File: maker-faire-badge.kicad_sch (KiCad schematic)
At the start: 37 parts, among them J1 USB-C, Q1 2N3906, Q2 2N3906, Q3 2N3906, Q4 2N3906, Q5 2N3906, Q6 2N3906

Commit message: updated design files
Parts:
- BT1, BT2: symbol Device:Battery_Cell -> Library:Battery_Cell
- C1, C2, C3, C4, C5, C6: symbol Device:C_Polarized_US -> Library:C_Polarized_US
- D1: symbol Device:LED_BKRG -> Library:LED_BKRG
- D2: symbol Device:D_Zener -> Library:D_Zener
- D3, D4: symbol Diode:1N5822 -> Library:1N5822
- H1: symbol Mechanical:MountingHole_Pad -> Library:MountingHole_Pad
- J1: symbol Connector:USB_C_Receptacle_PowerOnly_6P -> Library:USB_C_Receptacle_PowerOnly_6P
- Q1, Q2, Q3, Q4, Q5, Q6: symbol Transistor_BJT:2N3906 -> Library:2N3906
- R1: value 59.2k -> 15.4k; symbol Device:R_US -> Library:R_US; PartNumber MFR-25FBF52-56K2 -> MFR-25FBF52-15K4
- R10: value 40.2k -> 14k; symbol Device:R_US -> Library:R_US; PartNumber MFR-25FBF52-40K2 -> MFR-25FBF52-14K0
- R11, R2, R5: symbol Device:R_US -> Library:R_US; PartNumber MFR-25FRF52-205R -> MFR-25FBF52-205R
- R12: value 14k -> 40.2k; symbol Device:R_US -> Library:R_US; PartNumber MFR-25FBF52-14K0 -> MFR-25FBF52-40K2
- R13: symbol Device:R_US -> Library:R_US; PartNumber MFR-25FRF52-20R5 -> MFR-25FBF52-20R5
- R14, R16: symbol Device:R_US -> Library:R_US; PartNumber MFR-25FRF52-133R -> MFR-25FBF52-133R; now in the parts list
- R15: symbol Device:R_US -> Library:R_US; PartNumber MFR-25FRF52-205R -> MFR-25FBF52-205R; now in the parts list
- R17: symbol Device:R_US -> Library:R_US; now in the parts list
- R3: value 15.4k -> 59.2k; symbol Device:R_US -> Library:R_US; PartNumber MFR-25FBF52-15K4 -> MFR-25FBF52-56K2
- R4: value 48.7k -> 14.7k; symbol Device:R_US -> Library:R_US; PartNumber MFR-25FBF52-48K7 -> MFR-25FBF52-14K7
- R6: value 14.7k -> 48.7k; symbol Device:R_US -> Library:R_US; PartNumber MFR-25FBF52-14K7 -> MFR-25FBF52-48K7
- R7, R9: symbol Device:R_US -> Library:R_US; PartNumber MFR-25FRF52-24R9 -> MFR-25FBF52-24R9
- R8: symbol Device:R_US -> Library:R_US; PartNumber MFR-25FRF52-95R3 -> MFR-25FBF52-95R3
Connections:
- net BASE-1A: now also R3.2; no longer R3.1
- net BASE-1B: now also R1.2; no longer R1.1
- net BASE-2A: now also R6.2; no longer R6.1
- net BASE-2B: now also R4.2; no longer R4.1
- net BASE-3A: now also R12.2; no longer R12.1
- net BASE-3B: now also R10.2; no longer R10.1
- net GND: now also R1.1, R10.1, R11.1, R12.1, R2.1, R3.1, R4.1, R5.1, R6.1; no longer R1.2, R10.2, R11.2, R12.2, R2.2, R3.2, R4.2, R5.2, R6.2
- net at C5.2, Q5.3 (C): now also R11.2; no longer R11.1
- net at C1.2, Q1.3 (C): now also R2.2; no longer R2.1
- net at C3.2, Q3.3 (C): now also R5.2; no longer R5.1
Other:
- note added: "Board is designed to be powered by different sources, two coin cell batteries in series or a USB connector. R17 must not be populated when D4 is populated. This population will cause USB Power to feed into the coin cell batteries if when both batteries are dead installed and both batteries are dead. When D3 and D4 are populated, the power source with the higher voltage will power the board. When 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"
- note removed: "Board is designed to be powered by different sources, two coin cell batteries in series or a USB connector. When D3 and D4 are populated, the power source with the higher voltage will power the board. When R17 is populated, the coin cells will power the board. R17 must not be populated when D4 and 1 are populated. This population will cause USB Power to feed into the coin cell batteries."
- note removed: "LED Transistor"
- title: Maker Faire Orange County Badge Full Feature Assembly -> Maker Faire Orange County Badge
- moved on the sheet: D1, H1, R1, R10, R11, R12, R14, R15, R16, R17, R2, R3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

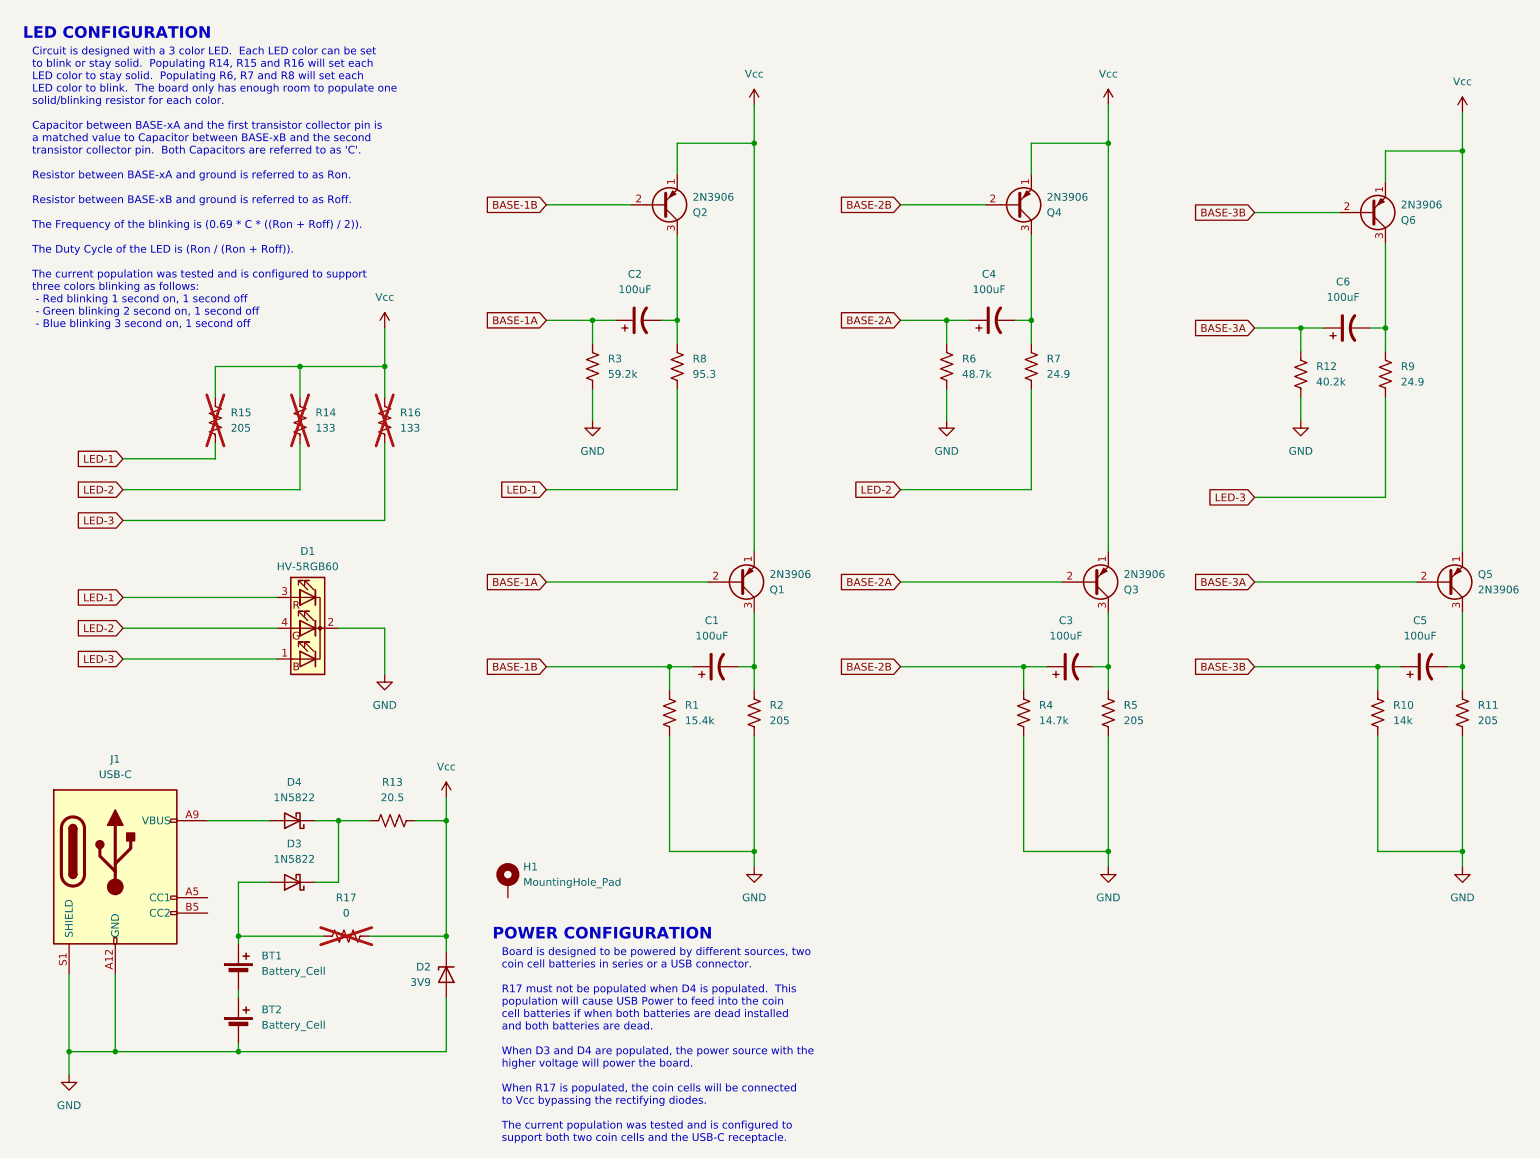
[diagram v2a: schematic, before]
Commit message: Initial design if Acylic Display PCBA
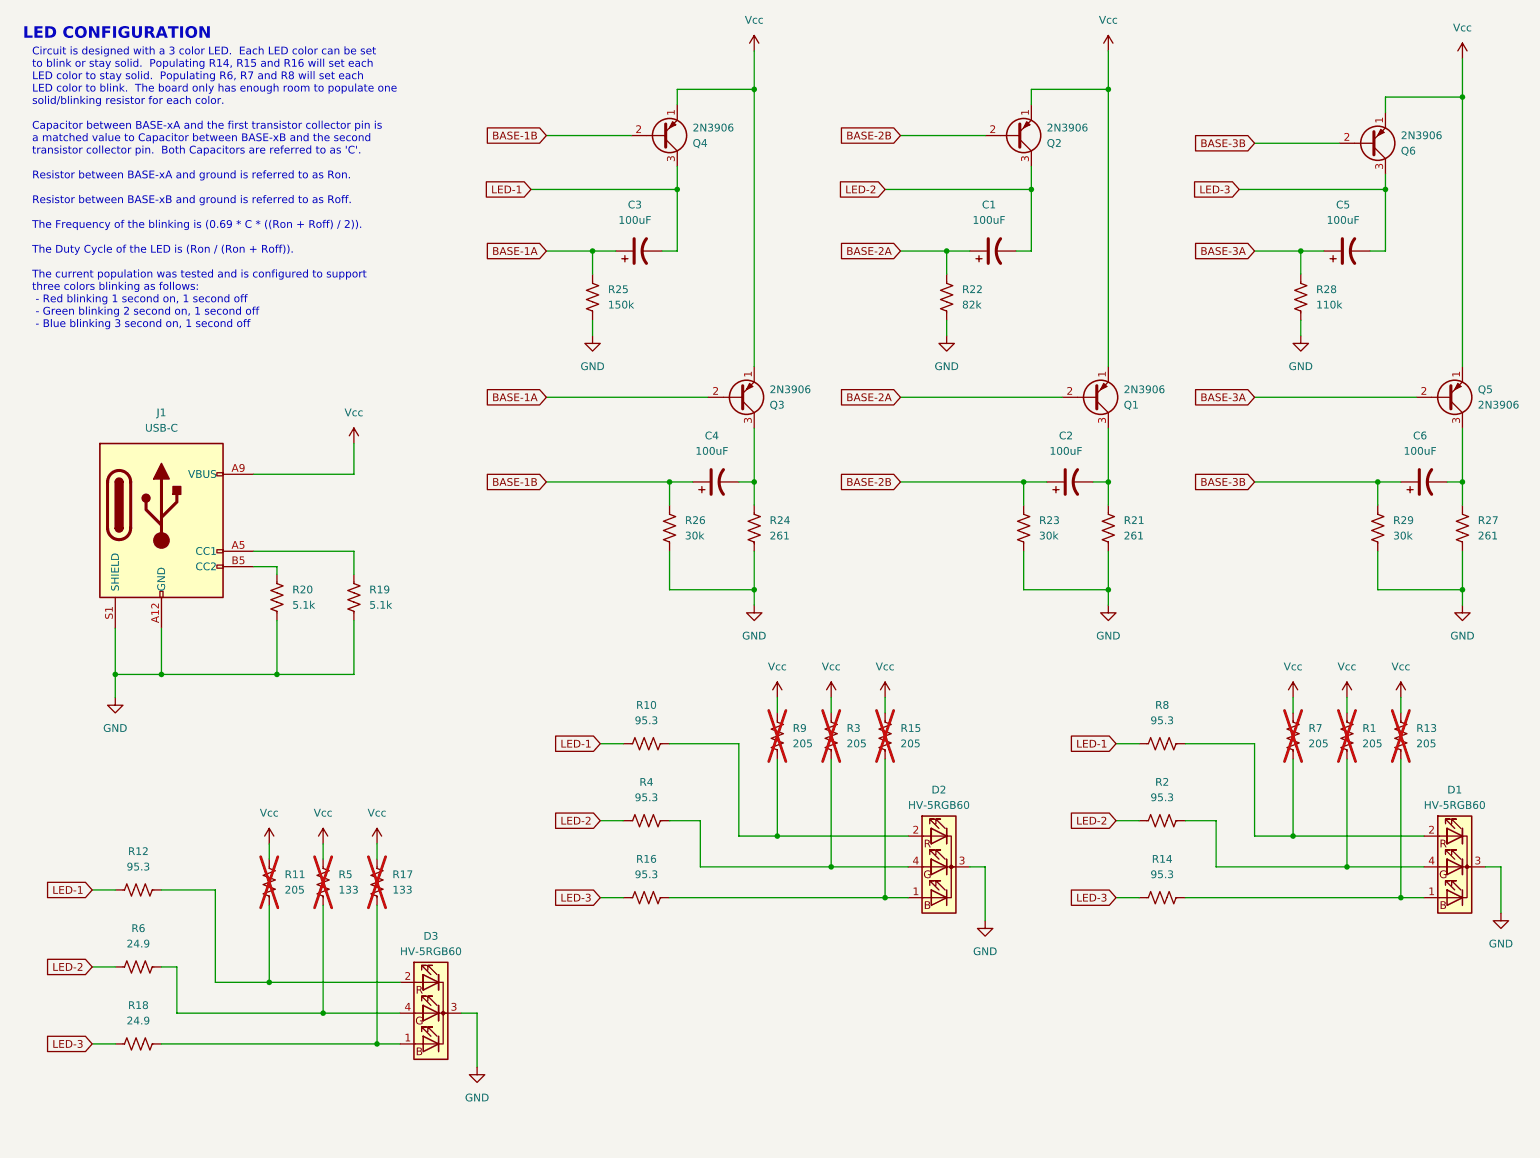
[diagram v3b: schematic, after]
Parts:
- removed BT1, BT2: Battery_Cell, Library:BAT_1074, symbol Library:Battery_Cell
- removed D2: 3V9, Diode_THT:D_DO-35_SOD27_P3.81mm_Vertical_KathodeUp, symbol Library:D_Zener
- removed D3, D4: 1N5822, Diode_THT:D_DO-201AD_P3.81mm_Vertical_KathodeUp, symbol Library:1N5822
- removed H1: MountingHole_Pad, MountingHole:MountingHole_3.2mm_M3_Pad_Via, symbol Library:MountingHole_Pad
- removed R17: 0, Resistor_THT:R_Axial_DIN0207_L6.3mm_D2.5mm_P10.16mm_Horizontal, symbol Library:R_US
- added D1, D2: HV-5RGB60, LED_THT:LED_D5.0mm-4_RGB_Wide_Pins, symbol Device:LED_BRKG
- added R1, R15, R3, R7, R9: 205, Resistor_THT:R_Axial_DIN0207_L6.3mm_D2.5mm_P2.54mm_Vertical, symbol Library:R_US
- added R10, R14, R16, R2, R4, R8: 95.3, Resistor_THT:R_Axial_DIN0207_L6.3mm_D2.5mm_P2.54mm_Vertical, symbol Library:R_US
- added R19, R20: 5.1k, Resistor_THT:R_Axial_DIN0207_L6.3mm_D2.5mm_P2.54mm_Vertical, symbol Library:R_US
- D3: renamed from D1; symbol Library:LED_BKRG -> Device:LED_BRKG
- J1: footprint Connector_USB:USB_C_Receptacle_GCT_USB4125-xx-x-0190_6P_TopMnt_Horizontal -> Connector_USB:USB_C_Receptacle_GCT_USB4135-GF-A_6P_TopMnt_Horizontal; Manufacturer GCT -> FCI; PartNumber USB4125-GF-A-0190 -> 10174819-00011LF
- R11: renamed from R15; footprint Resistor_THT:R_Axial_DIN0207_L6.3mm_D2.5mm_P7.62mm_Horizontal -> Resistor_THT:R_Axial_DIN0207_L6.3mm_D2.5mm_P2.54mm_Vertical
- R13: value 20.5 -> 205; footprint Resistor_THT:R_Axial_DIN0207_L6.3mm_D2.5mm_P10.16mm_Horizontal -> Resistor_THT:R_Axial_DIN0207_L6.3mm_D2.5mm_P2.54mm_Vertical; PartNumber MFR-25FBF52-20R5 -> MFR-25FBF52-205R; now not fitted
- R17: renamed from R16; footprint Resistor_THT:R_Axial_DIN0207_L6.3mm_D2.5mm_P7.62mm_Horizontal -> Resistor_THT:R_Axial_DIN0207_L6.3mm_D2.5mm_P2.54mm_Vertical
- R21: renamed from R5; value 205 -> 261; PartNumber MFR-25FBF52-205R -> MFR-25FBF52-261R
- R22: renamed from R6; value 48.7k -> 82k; Manufacturer Yageo -> YAGEO; PartNumber MFR-25FBF52-48K7 -> CFR-25JR-52-82K
- R23: renamed from R4; value 14.7k -> 30k; PartNumber MFR-25FBF52-14K7 -> CFR-25JR-52-30K
- R24: renamed from R2; value 205 -> 261; PartNumber MFR-25FBF52-205R -> MFR-25FBF52-261R
- R25: renamed from R3; value 59.2k -> 150k; Manufacturer Yageo -> TE Connectivity; PartNumber MFR-25FBF52-56K2 -> CFR-25JR-52-150K
- R26: renamed from R1; value 15.4k -> 30k; PartNumber MFR-25FBF52-15K4 -> CFR-25JR-52-30K
- R27: renamed from R11; value 205 -> 261; PartNumber MFR-25FBF52-205R -> MFR-25FBF52-261R
- R28: renamed from R12; value 40.2k -> 110k; PartNumber MFR-25FBF52-40K2 -> CFR-25JR-52-110K
- R29: renamed from R10; value 14k -> 30k; PartNumber MFR-25FBF52-14K0 -> CFR-25JR-52-30K
- R5: renamed from R14; footprint Resistor_THT:R_Axial_DIN0207_L6.3mm_D2.5mm_P7.62mm_Horizontal -> Resistor_THT:R_Axial_DIN0207_L6.3mm_D2.5mm_P2.54mm_Vertical
- renumbered C4 to C1, C3 to C2, C2 to C3, C1 to C4, C6 to C5, C5 to C6, Q3 to Q1, Q4 to Q2, Q1 to Q3, Q2 to Q4, R8 to R12, R9 to R18, R7 to R6
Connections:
- net GND: now also D3.3 (K), D1.3 (K), D2.3 (K), R19.1, R20.1; no longer D3.2 (K)
- net LED-1: now also C3.2, Q4.3 (C), R10.2, R8.2; no longer D3.3 (RA), R11.2
- net LED-2: now also C1.2, Q2.3 (C), R2.2, R4.2; no longer D3.4 (GA), R5.2
- net LED-3: now also C5.2, Q6.3 (C), R14.2, R16.2; no longer D3.1 (BA), R17.2
- net Vcc: now also J1.A9 (VBUS), J1.B9 (VBUS), R11.2, R17.2, R5.2, R1.2, R15.2, R3.2, R7.2, R9.2; no longer R11.1, R17.1, R5.1
- net at R13.1: now also D1.1 (BA), R14.1
- net at J1.A5 (CC1): now also R19.2
- net at J1.B5 (CC2): now also R20.2
- new net: D1.4 (GA), R1.1, R2.1
- new net: D2.4 (GA), R3.1, R4.1
- new net: D1.2 (RA), R7.1, R8.1
- new net: D2.1 (BA), R15.1, R16.1
- new net: D3.1 (BA), R17.1, R18.1
- new net: D2.2 (RA), R10.1, R9.1
- new net: D3.2 (RA), R11.1, R12.1
- new net: D3.4 (GA), R5.1, R6.1
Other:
- note removed: "Board is designed to be powered by different sources, two coin cell batteries in series or a USB connector. R17 must not be populated when D4 is populated. This population will cause USB Power to feed into the coin cell batteries if when both batteries are dead installed and both batteries are dead. When D3 and D4 are populated, the power source with the higher voltage will power the board. When 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"
- note removed: "POWER CONFIGURATION"
- moved on the sheet: C1, C2, C3, C4, C5, C6, D3, Q1, Q2, Q3, Q4, Q5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
